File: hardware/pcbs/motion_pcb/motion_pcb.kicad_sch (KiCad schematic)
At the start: 23 parts, among them J1 esp_io_shield1, J2 esp_io_shield2, J3 esp32_voltage_shield, J4 Con_top_pcb, J5 con_rpi, SW1 SW_Push, U4 74HC4051

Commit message: finished schematic
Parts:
- removed C3, C4: 100nF, Capacitor_SMD:C_1206_3216Metric_Pad1.33x1.80mm_HandSolder, symbol Device:C
- removed J1: esp_io_shield1, Connector_PinHeader_2.54mm:PinHeader_2x07_P2.54mm_Vertical_SMD, symbol Connector_Generic:Conn_02x07_Odd_Even
- removed J2: esp_io_shield2, Connector_PinHeader_2.54mm:PinHeader_2x11_P2.54mm_Vertical_SMD, symbol Connector_Generic:Conn_02x11_Odd_Even
- removed J3: esp32_voltage_shield, Connector_PinHeader_2.54mm:PinHeader_2x04_P2.54mm_Vertical_SMD, symbol Connector_Generic:Conn_02x04_Odd_Even
- removed J4: Con_top_pcb, Connector_JST:JST_PH_B9B-PH-K_1x09_P2.00mm_Vertical, symbol Connector:Conn_01x09_Pin
- removed J5: con_rpi, Connector_JST:JST_PH_B9B-PH-K_1x09_P2.00mm_Vertical, symbol Connector:Conn_01x09_Pin
- removed R1, R2, R3, R4, R6, R7, R8: 100, Resistor_SMD:R_1206_3216Metric_Pad1.30x1.75mm_HandSolder, symbol Device:R
- removed SW1: SW_Push, symbol Switch:SW_Push
- removed U2: ~, esp32:DFR0645, symbol esp32:DFR0654
- removed U4: 74HC4051, Package_SO:SOIC-16_3.9x9.9mm_P1.27mm, symbol 74xx:74HC4051
- added C5: 10v/1mF, Capacitor_SMD:CP_Elec_10x10, symbol Device:C_Polarized
- added J1: Conn_02x16_Odd_Even, symbol Connector_Generic:Conn_02x16_Odd_Even
- added J2: Conn_02x06_Odd_Even, symbol Connector_Generic:Conn_02x06_Odd_Even
- added J3: Conn_02x02_Odd_Even, symbol Connector_Generic:Conn_02x02_Odd_Even
- added J4: Conn_02x01, symbol Connector_Generic:Conn_02x01
- added U2: ~, 3dAudioFoot:ESP32-S3-DevKitC-1, symbol 3dAudioSym:ESP32_S3_DevKit_C1
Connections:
- net +3V3: now also J3.1 (Pin_1), J3.2 (Pin_2), U2.1 (3v3), U2.2 (3v3)
- net +5V: now also C5.1, U2.21 (5V)
- net EA1: now also J1.29 (Pin_29), J1.30 (Pin_30), U2.19 (IO13/AD2_2)
- net EA2: now also J1.21 (Pin_21), J1.22 (Pin_22), U2.15 (IO9/AD1_8)
- net EA3: now also J1.10 (Pin_10), J1.9 (Pin_9), U2.8 (IO15/AD2_4)
- net EA4: now also J1.1 (Pin_1), J1.2 (Pin_2), U2.4 (IO4/AD1_3)
- net EB1: now also J1.31 (Pin_31), J1.32 (Pin_32), U2.20 (IO14/AD2_3)
- net EB2: now also J1.23 (Pin_23), J1.24 (Pin_24), U2.16 (IO10/AD1_9)
- net EB3: now also J1.11 (Pin_11), J1.12 (Pin_12), U2.9 (IO16/AD2_5)
- net EB4: now also J1.3 (Pin_3), J1.4 (Pin_4), U2.5 (IO5/AD1_4)
- net GND: now also C5.2, J3.3 (Pin_3), U2.22 (GND), U2.23 (GND), U2.24 (GND)
- net MUX_A: now also J2.7 (Pin_7), J2.8 (Pin_8), U2.37 (IO40)
- net MUX_B: now also J2.10 (Pin_10), J2.9 (Pin_9), U2.36 (IO39)
- net MUX_C: now also J2.11 (Pin_11), J2.12 (Pin_12), U2.35 (IO38/LED)
- net MUX_S0: now also J2.5 (Pin_5), J2.6 (Pin_6), U2.38 (IO41)
- net MUX_S1: now also J2.3 (Pin_3), J2.4 (Pin_4), U2.39 (IO42)
- net MUX_S2: now also J2.1 (Pin_1), J2.2 (Pin_2), U2.40 (IO2/AD1_1)
- net led_dat: now also J4.1 (Pin_1), J4.2 (Pin_2), U2.27 (IO21)
- new net: J3.4 (Pin_4), U2.3 (RST)
- new net PT11: J1.25 (Pin_25), J1.26 (Pin_26), U2.17 (IO11/AD2_0)
- new net PT12: J1.17 (Pin_17), J1.18 (Pin_18), U2.12 (IO8/AD1_7)
- new net PT13: J1.15 (Pin_15), J1.16 (Pin_16), U2.11 (IO18/AD2_7)
- new net PT14: J1.7 (Pin_7), J1.8 (Pin_8), U2.7 (IO7/AD1_6)
- new net PT21: J1.27 (Pin_27), J1.28 (Pin_28), U2.18 (IO12/AD2_1)
- new net PT22: J1.19 (Pin_19), J1.20 (Pin_20), U2.13 (IO3/AD1_2)
- new net PT23: J1.13 (Pin_13), J1.14 (Pin_14), U2.10 (IO17/AD2_6)
- new net PT24: J1.5 (Pin_5), J1.6 (Pin_6), U2.6 (IO6/AD1_5)
- no-connect marks 15 -> 6
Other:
- added sheet poti_arr (poti_arr.kicad_sch)
- sheet Button square ports: added B11, B12, B13, B14, B21, B22, B23, B24, B31, B32, B33, B34, B41, B42, B43, B44, BR1, BR2, BR3, C, ES1, ES2, ES3, ES4; removed none
- sheet LED ports: added LED_DAT, LED_DAT_OUT, SW11, SW12, SW13, SW14, SW21, SW22, SW23, SW24, SW31, SW32, SW33, SW34, SW41, SW42, SW43, SW44; removed led_dat
- sheet button round ports: added BR1, BR2, BR3, LED_DAT; removed but_rnd1, but_rnd2, but_rnd3
- moved on the sheet: H1, H2, H3, H4, H5, H6

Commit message: cleanup led driver
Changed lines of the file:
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@@
+	(wire
+		(pts
+			(xy 248.92 24.13) (xy 233.68 24.13)
+		)
+		(stroke
+			(width 0)
+			(type default)
+		)
+	)
 	(wire
 		(pts
@@
 	(wire
 		(pts
+			(xy 214.63 96.52) (xy 219.71 96.52)
+		)
+		(stroke
+			(width 0)
+			(type default)
+		)
+	)
+	(wire
+		(pts
 			(xy 44.45 55.88) (xy 58.42 55.88)
 		)
@@
 	(global_label "led_dat2"
 		(shape input)
-		(at 219.71 96.52 180)
-		(fields_autoplaced yes)
-		(effects
-			(font
-				(size 1.27 1.27)
-			)
-			(justify right)
-		)
-		(property "Intersheetrefs" "${INTERSHEET_REFS}"
-			(at 208.6212 96.52 0)
+		(at 214.63 96.52 180)
+		(fields_autoplaced yes)
+		(effects
+			(font
+				(size 1.27 1.27)
+			)
+			(justify right)
+		)
+		(property "Intersheetrefs" "${INTERSHEET_REFS}"
+			(at 203.5412 96.52 0)
 			(effects
 				(font
@@
 	(global_label "led_dat2"
 		(shape input)
-		(at 233.68 24.13 0)
+		(at 248.92 24.13 0)
 		(fields_autoplaced yes)
 		(effects
@@
 		)
 		(property "Intersheetrefs" "${INTERSHEET_REFS}"
-			(at 244.7688 24.13 0)
+			(at 260.0088 24.13 0)
 			(effects
 				(font
@@
 		(length 1)
 		(shape round)
-		(at 214.4206 20.4157 0)
+		(at 241.3 24.13 0)
 		(effects
 			(font
@@
 		)
 		(property "Netclass" "HIF"
-			(at 213.9126 19.3997 0)
-			(effects
-				(font
+			(at 240.792 23.114 0)
+			(effects
+				(font
+					(size 1.27 1.27)
+					(italic yes)
+				)
+				(justify right)
+			)
+		)
+	)
+	(netclass_flag ""
+		(length 1)
+		(shape round)
+		(at 157.48 20.32 0)
+		(effects
+			(font
+				(size 1.27 1.27)
+			)
+			(justify left bottom)
+		)
+		(property "Netclass" "HIF"
+			(at 156.972 19.304 0)
+			(effects
+				(font
+					(size 1.27 1.27)
+					(italic yes)
+				)
+				(justify right)
+			)
+		)
+	)
+	(netclass_flag ""
+		(length 1)
+		(shape round)
+		(at 214.63 20.32 0)
+		(effects
+			(font
+				(size 1.27 1.27)
+			)
+			(justify left bottom)
+		)
+		(property "Netclass" "HIF"
+			(at 214.122 19.304 0)
+			(effects
+				(font

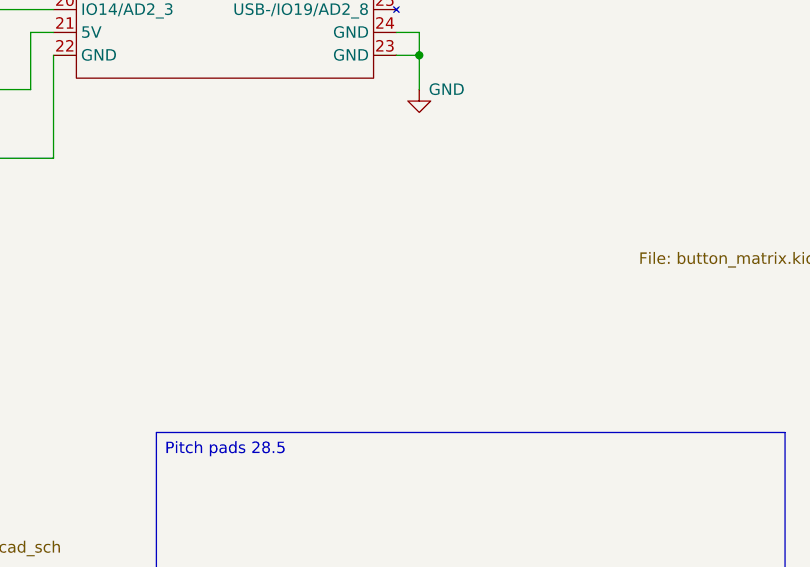
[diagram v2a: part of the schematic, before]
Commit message: created submodule for enc pot mix
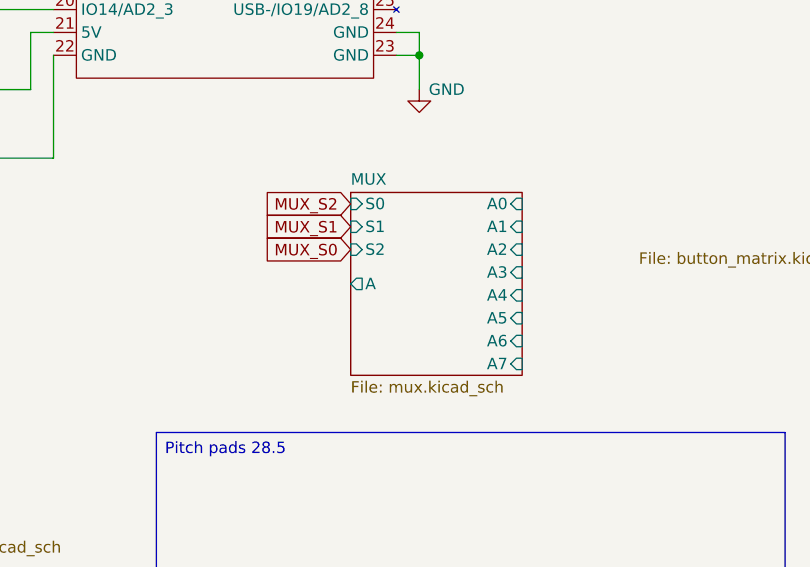
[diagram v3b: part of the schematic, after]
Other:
- added sheet MUX (mux.kicad_sch)
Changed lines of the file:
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@@
+		)
+	)
+	(global_label "MUX_S2"
+		(shape input)
+		(at 95.25 95.25 180)
+		(fields_autoplaced yes)
+		(effects
+			(font
+				(size 1.27 1.27)
+			)
+			(justify right)
+		)
+		(property "Intersheetrefs" "${INTERSHEET_REFS}"
+			(at 84.8868 95.25 0)
+			(effects
+				(font
+					(size 1.27 1.27)
+				)
+				(justify right)
+				(hide yes)
+			)
 		)
 	)
@@
 		)
 	)
+	(global_label "MUX_S0"
+		(shape input)
+		(at 95.25 100.33 180)
+		(fields_autoplaced yes)
+		(effects
+			(font
+				(size 1.27 1.27)
+			)
+			(justify right)
+		)
+		(property "Intersheetrefs" "${INTERSHEET_REFS}"
+			(at 84.8868 100.33 0)
+			(effects
+				(font
+					(size 1.27 1.27)
+				)
+				(justify right)
+				(hide yes)
+			)
+		)
+	)
 	(global_label "MUX_C"
 		(shape input)
@@
 		(property "Intersheetrefs" "${INTERSHEET_REFS}"
 			(at 35.5382 129.54 0)
+			(effects
+				(font
+					(size 1.27 1.27)
+				)
+				(justify right)
+				(hide yes)
+			)
+		)
+	)
+	(global_label "MUX_S1"
+		(shape input)
+		(at 95.25 97.79 180)
+		(fields_autoplaced yes)
+		(effects
+			(font
+				(size 1.27 1.27)
+			)
+			(justify right)
+		)
+		(property "Intersheetrefs" "${INTERSHEET_REFS}"
+			(at 84.8868 97.79 0)
 			(effects
 				(font
@@
 				)
 			)
+		)
+	)
+	(sheet
+		(at 95.25 93.98)
+		(size 19.05 20.32)
+		(exclude_from_sim no)
+		(in_bom yes)
+		(on_board yes)
+		(dnp no)
+		(fields_autoplaced yes)
+		(stroke
+			(width 0.1524)
+			(type solid)
+		)
+		(fill
+			(color 0 0 0 0.0000)
+		)
+		(property "Sheetname" "MUX"
+			(at 95.25 93.2684 0)
+			(effects
+				(font
+					(size 1.27 1.27)
+				)
+				(justify left bottom)
+			)
+		)
+		(property "Sheetfile" "mux.kicad_sch"
+			(at 95.25 114.8846 0)
+			(effects
+				(font
+					(size 1.27 1.27)
+				)
+				(justify left top)
+			)
+		)
+		(property "Field2" ""
+			(at 95.25 93.98 0)
+			(effects
+				(font
+					(size 1.27 1.27)
+				)
+			)
+		)
+		(pin "A3" input
+			(at 114.3 102.87 0)
+			(effects
+				(font
+					(size 1.27 1.27)
+				)
+				(justify right)
+			)
+		)
+		(pin "A4" input
+			(at 114.3 105.41 0)
+			(effects
+				(font
+					(size 1.27 1.27)
+				)
+				(justify right)
+			)
+		)
+		(pin "A" output
+			(at 95.25 104.14 180)
+			(effects
+				(font
+					(size 1.27 1.27)
+				)
+				(justify left)
+			)
+		)
+		(pin "A5" input
+			(at 114.3 107.95 0)
+			(effects
+				(font
+					(size 1.27 1.27)
+				)
+				(justify right)
+			)
+		)
+		(pin "A1" input
+			(at 114.3 97.79 0)
+			(effects
+				(font
+					(size 1.27 1.27)
+				)
+				(justify right)
+			)
+		)
+		(pin "S1" input
+			(at 95.25 97.79 180)
+			(effects
+				(font
+					(size 1.27 1.27)
+				)
+				(justify left)
+			)
+		)
+		(pin "A2" input
+			(at 114.3 100.33 0)
+			(effects
+				(font
+					(size 1.27 1.27)
+				)
+				(justify right)
+			)
+		)
+		(pin "S0" input
+			(at 95.25 95.25 180)
+			(effects
+				(font
+					(size 1.27 1.27)
+				)
+				(justify left)
+			)
+		)
+		(pin "A7" input
+			(at 114.3 113.03 0)
+			(effects
+				(font
+					(size 1.27 1.27)
+				)
+				(justify right)
+			)
+		)
+		(pin "A0" input
+			(at 114.3 95.25 0)
+			(effects
+				(font
+					(size 1.27 1.27)
+				)
+				(justify right)
+			)
+		)
+		(pin "A6" input
+			(at 114.3 110.49 0)
+			(effects
+				(font
+					(size 1.27 1.27)
+				)
+				(justify right)
+			)
+		)
+		(pin "S2" input
+			(at 95.25 100.33 180)
+			(effects
+				(font
+					(size 1.27 1.27)
+				)
+				(justify left)
+			)
+		)
+		(instances
+			(project "motion_pcb"
+				(path "/1501dcbd-05c1-4298-b373-c91a1b0991c0"
+					(page "39")
+				)
+			)

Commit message: changing labels
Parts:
- J1: renamed from J3; footprint (none) -> Connector_PinHeader_2.54mm:PinHeader_2x02_P2.54mm_Vertical
- J2: footprint (none) -> Connector_PinHeader_2.54mm:PinHeader_2x06_P2.54mm_Vertical
- J3: renamed from J1; footprint (none) -> Connector_PinHeader_2.54mm:PinHeader_2x16_P2.54mm_Vertical
- J4: footprint (none) -> Connector_PinHeader_2.54mm:PinHeader_1x02_P2.54mm_Vertical
- renumbered C5 to C1, U2 to IC1
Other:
- removed sheet Button square
- removed sheet Encoder
- removed sheet MUX
- removed sheet button round
- added sheet mux (mux.kicad_sch)
- sheet LED ports: added SW00, SW09, SW10, SW19, SW20, SW25, SW26, SW27, SW28, SW29, SW30, SW35, SW36, SW37, SW38, SW39, SW40, SW45, SW46, SW47, SW48, SW49, SW50, SW51, SW52, SW53, SW54, SW55, SW56, SW57, SW58, SW59; removed LED_DAT_OUT, SW11, SW12, SW13, SW14
- sheet led_driver ports: added none; removed in, out
- sheet poti_arr ports: added EA01, EA03, EA05, EA07, EA12, EA14, EA16, EA18, EA21, EA23, EA25, EA27, EB01, EB03, EB05, EB07, EB12, EB14, EB16, EB18, EB21, EB23, EB25, EB27, ES01, ES03, ES05, ES07, ES12, ES14, ES16, ES18, ES21, ES23, ES25, ES27; removed p11, p12, p13, p14, p21, p22, p23, p24

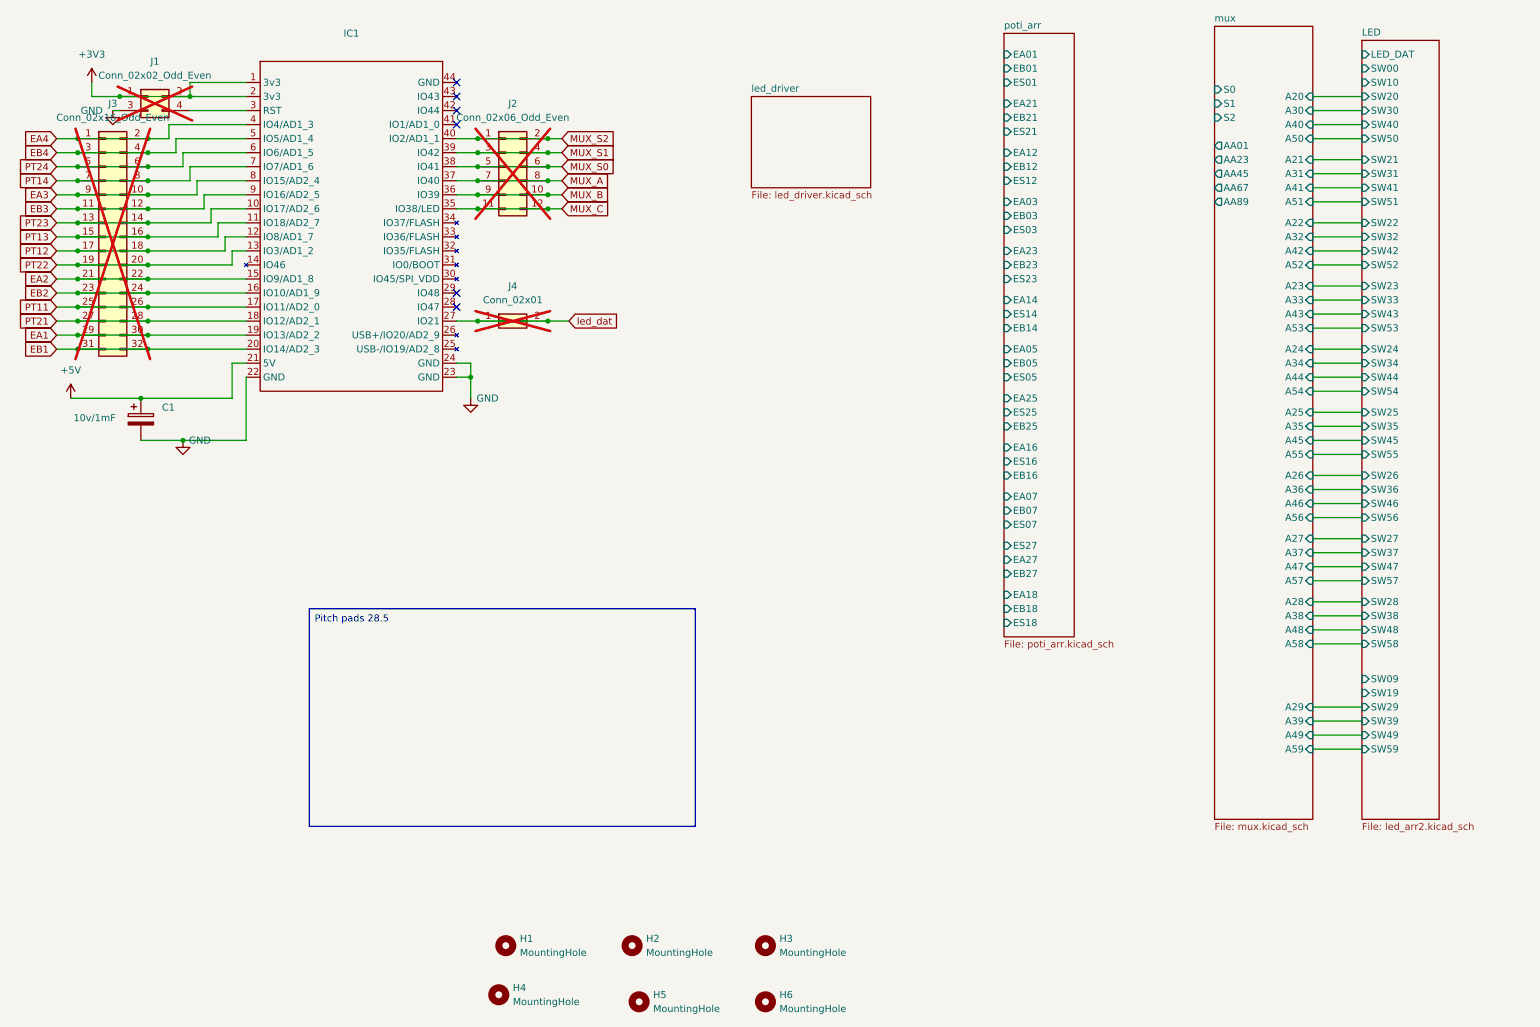
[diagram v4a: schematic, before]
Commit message: finished pcb motion.
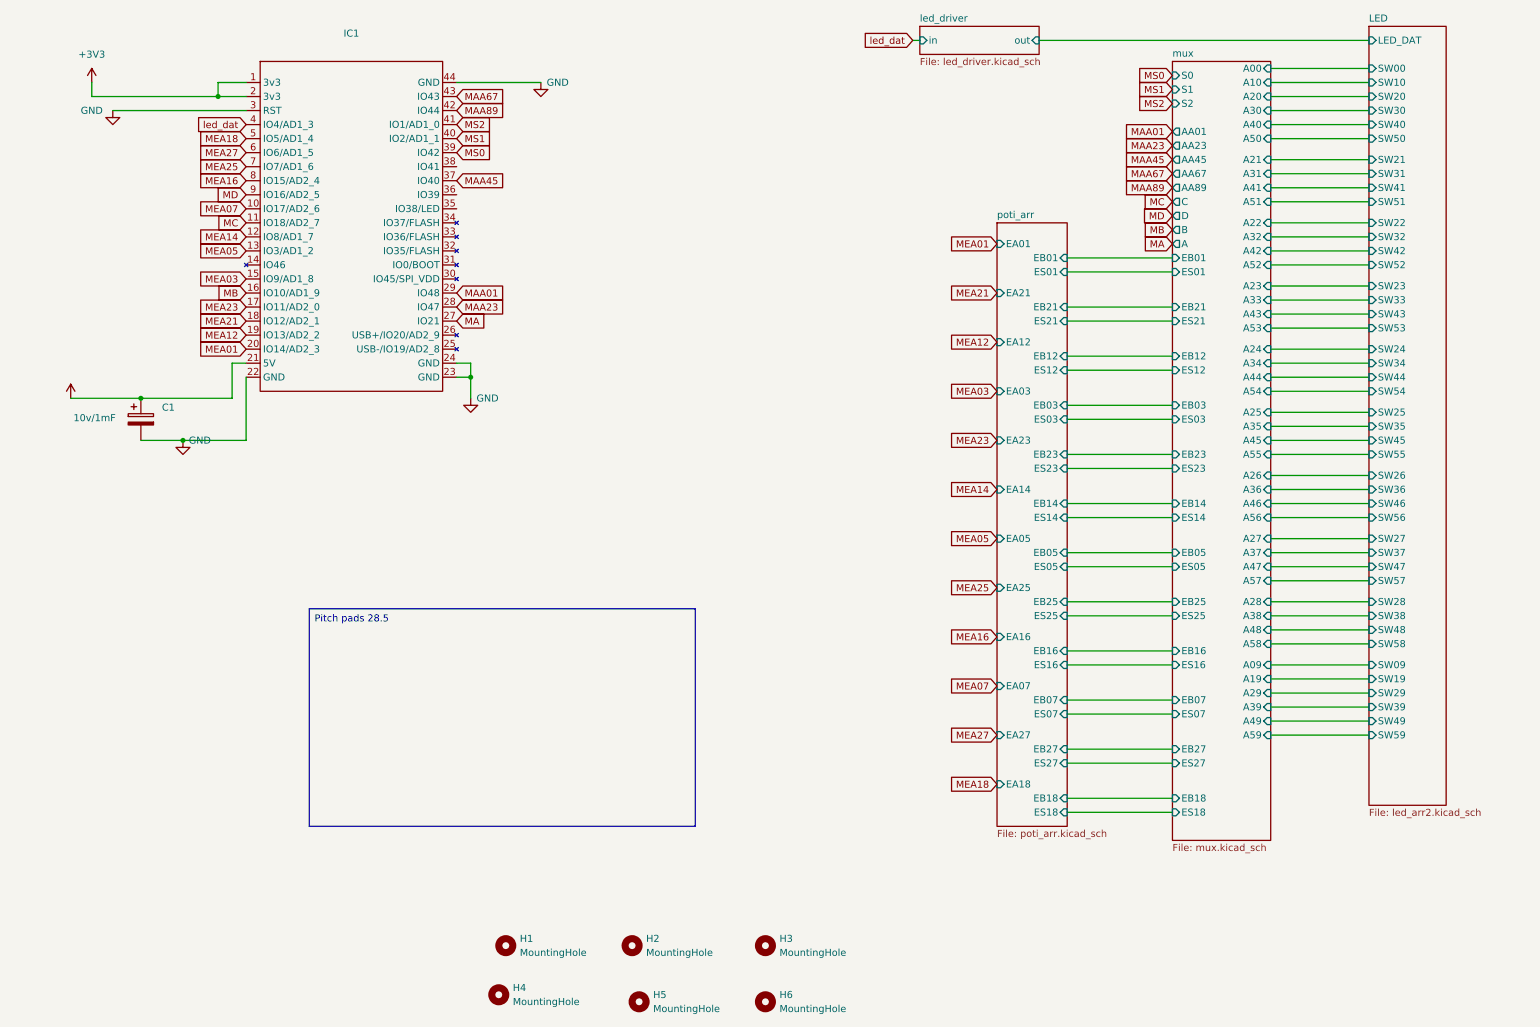
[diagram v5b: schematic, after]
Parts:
- removed J1: Conn_02x02_Odd_Even, Connector_PinHeader_2.54mm:PinHeader_2x02_P2.54mm_Vertical, symbol Connector_Generic:Conn_02x02_Odd_Even
- removed J2: Conn_02x06_Odd_Even, Connector_PinHeader_2.54mm:PinHeader_2x06_P2.54mm_Vertical, symbol Connector_Generic:Conn_02x06_Odd_Even
- removed J3: Conn_02x16_Odd_Even, Connector_PinHeader_2.54mm:PinHeader_2x16_P2.54mm_Vertical, symbol Connector_Generic:Conn_02x16_Odd_Even
- removed J4: Conn_02x01, Connector_PinHeader_2.54mm:PinHeader_1x02_P2.54mm_Vertical, symbol Connector_Generic:Conn_02x01
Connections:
- net EA4 is gone; now on net led_dat: IC1.4 (IO4/AD1_3)
- net GND: now also IC1.3 (RST), IC1.44 (GND)
- net led_dat: no longer IC1.27 (IO21)
- net MAA23: now reaches IC1.28 (IO47)
- net MAA01: now reaches IC1.29 (IO48)
- net MS2: now reaches IC1.41 (IO1/AD1_0)
- net MAA89: now reaches IC1.42 (IO44)
- net MAA67: now reaches IC1.43 (IO43)
- net EA1 renamed MEA12
- net EA2 renamed MEA03
- net EA3 renamed MEA16
- net EB1 renamed MEA01
- net EB2 renamed MB
- net EB3 renamed MD
- net EB4 renamed MEA18
- net MUX_A renamed MAA45
- net MUX_B: no longer names the net of IC1.36 (IO39)
- net MUX_C: no longer names the net of IC1.35 (IO38/LED)
- net MUX_S0: no longer names the net of IC1.38 (IO41)
- net MUX_S1 renamed MS0
- net MUX_S2 renamed MS1
- net PT11 renamed MEA23
- net PT12 renamed MEA14
- net PT13 renamed MC
- net PT14 renamed MEA25
- net PT21 renamed MEA21
- net PT22 renamed MEA05
- net PT23 renamed MEA07
- net PT24 renamed MEA27
- new net MA: IC1.27 (IO21)
- no-connect marks 6 -> 0
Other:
- sheet led_driver ports: added in, out; removed none
- sheet mux ports: added A, A00, A09, A10, A19, B, C, D, EB01, EB03, EB05, EB07, EB12, EB14, EB16, EB18, EB21, EB23, EB25, EB27, ES01, ES03, ES05, ES07, ES12, ES14, ES16, ES18, ES21, ES23, ES25, ES27; removed none

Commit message: finished design
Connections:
- net led_dat is gone; now on net MEA01: IC1.4 (IO4/AD1_3)
- net MA: now also IC1.40 (IO2/AD1_1); no longer IC1.27 (IO21)
- net MAA01: now also IC1.38 (IO41); no longer IC1.29 (IO48)
- net MAA23: now also IC1.39 (IO42); no longer IC1.28 (IO47)
- net MAA67: now also IC1.27 (IO21); no longer IC1.43 (IO43)
- net MAA89: now also IC1.28 (IO47); no longer IC1.42 (IO44)
- net MB: now also IC1.8 (IO15/AD2_4); no longer IC1.16 (IO10/AD1_9)
- net MC: now also IC1.12 (IO8/AD1_7); no longer IC1.11 (IO18/AD2_7)
- net MD: now also IC1.15 (IO9/AD1_8); no longer IC1.9 (IO16/AD2_5)
- net MEA01: no longer IC1.20 (IO14/AD2_3)
- net MEA03: now also IC1.9 (IO16/AD2_5); no longer IC1.15 (IO9/AD1_8)
- net MEA05: now also IC1.10 (IO17/AD2_6); no longer IC1.13 (IO3/AD1_2)
- net MEA07: now also IC1.13 (IO3/AD1_2); no longer IC1.10 (IO17/AD2_6)
- net MEA12: now also IC1.5 (IO5/AD1_4); no longer IC1.19 (IO13/AD2_2)
- net MEA14: now also IC1.11 (IO18/AD2_7); no longer IC1.12 (IO8/AD1_7)
- net MEA16: now also IC1.16 (IO10/AD1_9); no longer IC1.8 (IO15/AD2_4)
- net MEA18: now also IC1.19 (IO13/AD2_2); no longer IC1.5 (IO5/AD1_4)
- net MEA21: now also IC1.6 (IO6/AD1_5); no longer IC1.18 (IO12/AD2_1)
- net MEA23: now also IC1.7 (IO7/AD1_6); no longer IC1.17 (IO11/AD2_0)
- net MEA25: now also IC1.17 (IO11/AD2_0); no longer IC1.7 (IO7/AD1_6)
- net MEA27: now also IC1.18 (IO12/AD2_1); no longer IC1.6 (IO6/AD1_5)
- net MS0: now also IC1.36 (IO39); no longer IC1.39 (IO42)
- net MS1: now also IC1.35 (IO38/LED); no longer IC1.40 (IO2/AD1_1)
- net MS2: now also IC1.29 (IO48); no longer IC1.41 (IO1/AD1_0)
- new net Mled_dat: IC1.20 (IO14/AD2_3)
- no-connect marks 0 -> 3
